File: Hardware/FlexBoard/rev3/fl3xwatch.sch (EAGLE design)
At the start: 24 parts, among them J1 DISP

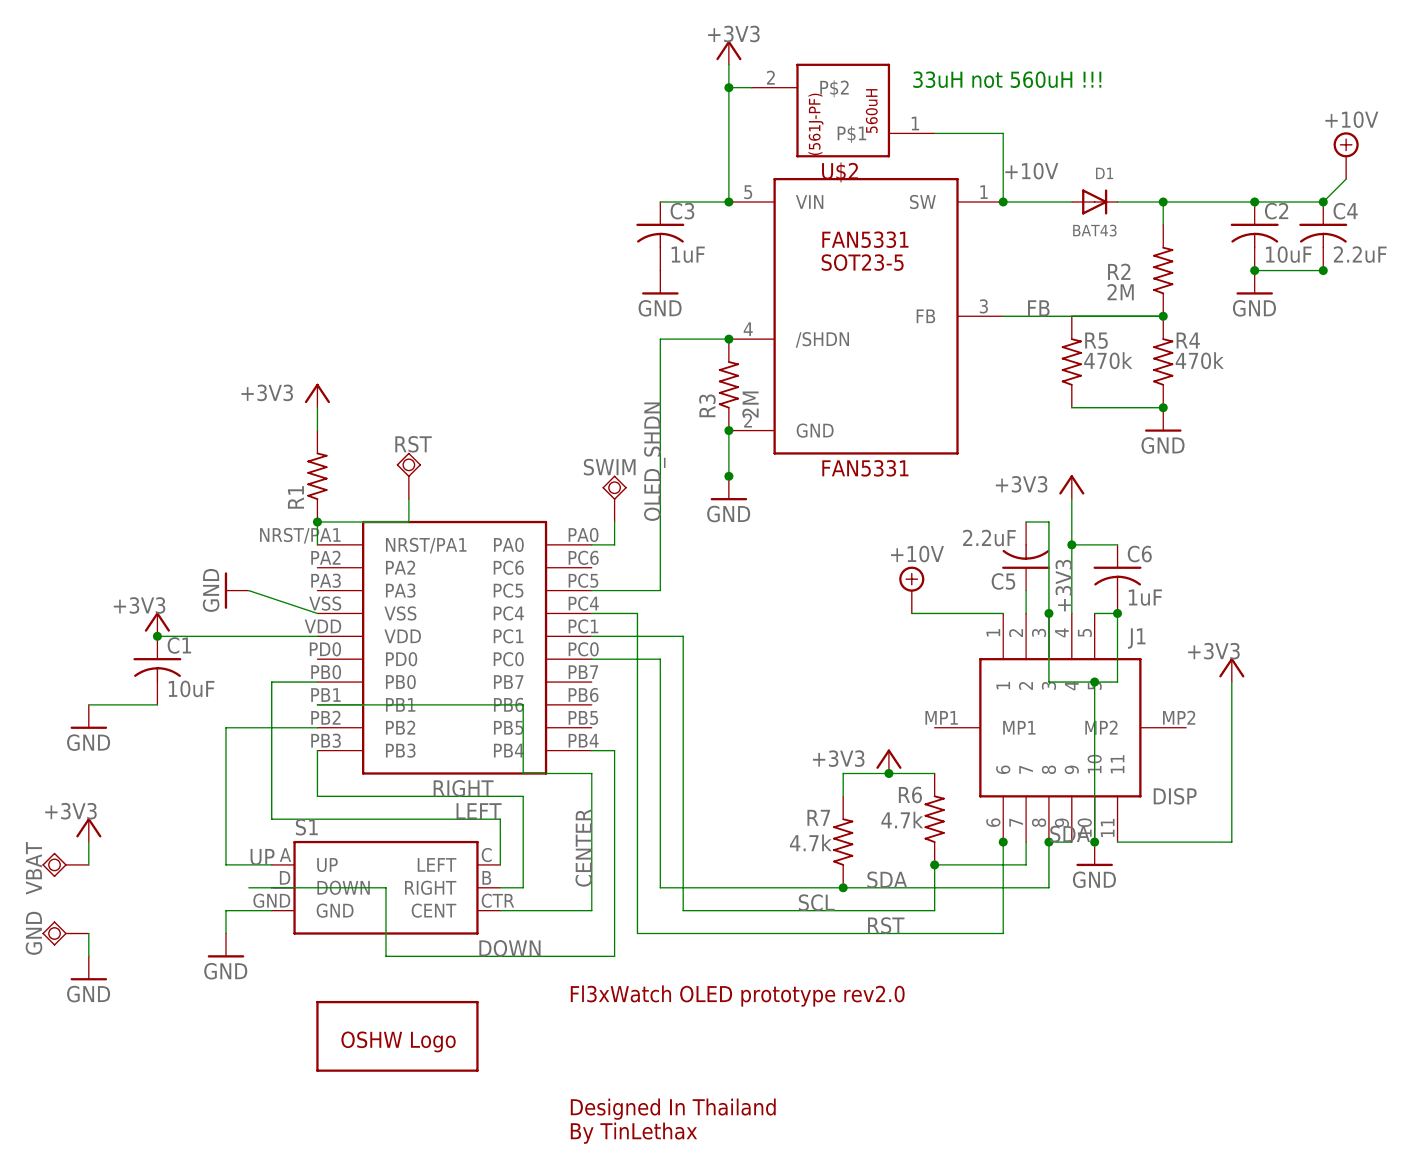
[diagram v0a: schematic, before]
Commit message: rev 2.1
corrected the inductor value. user
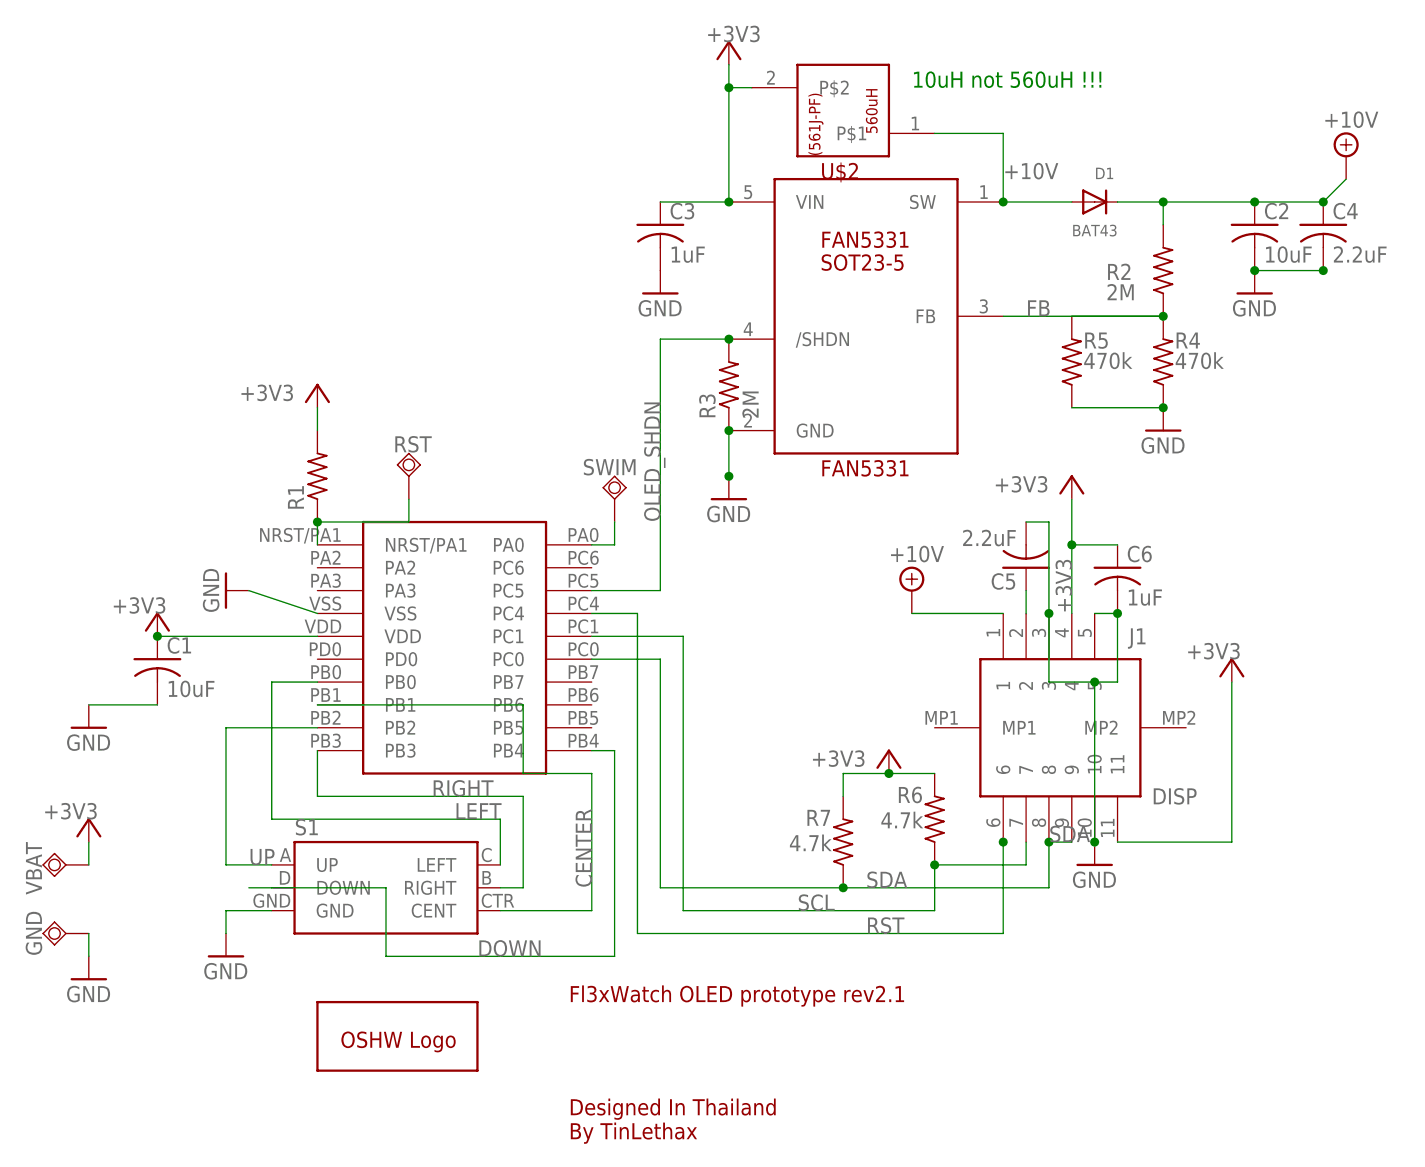
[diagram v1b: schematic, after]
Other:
- note added: "10uH not 560uH !!!"
- note added: "Fl3xWatch OLED prototype rev2.1"
- note removed: "33uH not 560uH !!!"
- note removed: "Fl3xWatch OLED prototype rev2.0"
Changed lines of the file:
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@@
 <setting verticaltext="up"/>
 </settings>
-<grid distance="0.1" unitdist="inch" unit="inch" style="lines" multiple="1" display="yes" altdistance="0.01" altunitdist="inch" altunit="inch"/>
+<grid distance="0.1" unitdist="inch" unit="inch" style="lines" multiple="1" display="no" altdistance="0.01" altunitdist="inch" altunit="inch"/>
 <layers>
 <layer number="1" name="Top" color="4" fill="1" visible="no" active="no"/>
@@
 <sheet>
 <plain>
-<text x="127" y="121.92" size="1.778" layer="91">33uH not 560uH !!!</text>
-<text x="88.9" y="20.32" size="1.778" layer="94">Fl3xWatch OLED prototype rev2.0</text>
+<text x="127" y="121.92" size="1.778" layer="91">10uH not 560uH !!!</text>
+<text x="88.9" y="20.32" size="1.778" layer="94">Fl3xWatch OLED prototype rev2.1</text>
 <text x="88.9" y="5.08" size="1.778" layer="94">Designed In Thailand
 By TinLethax</text>
